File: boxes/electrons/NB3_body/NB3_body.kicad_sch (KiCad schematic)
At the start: 21 parts, among them J1 Conn_01x02_Male, J2 Conn_01x02_Male, J3 Conn_01x02_Male, J4 Conn_01x02_Male, J5 Conn_01x04_Male, J6 Conn_01x02_Male

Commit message: Work on NB3_body PCB...
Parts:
- removed C3, C4, C5: 10uF, Capacitor_SMD:C_0805_2012Metric, symbol Device:C
- removed F3, F4, F6: 1.1h2.2t, Fuse:Fuse_0805_2012Metric, symbol Device:Polyfuse
- removed F5: 3h5t, Fuse:Fuse_2920_7451Metric, symbol Device:Polyfuse
- removed J1, J2, J3, J4, J6: Conn_01x02_Male, Connector_PinHeader_2.54mm:PinHeader_1x02_P2.54mm_Vertical_SMD_Pin1Right, symbol Connector:Conn_01x02_Male
- removed J5: Conn_01x04_Male, Connector_PinHeader_2.54mm:PinHeader_1x04_P2.54mm_Vertical_SMD_Pin1Right, symbol Connector:Conn_01x04_Male
- added J1, J10, J2, J9: Conn_01x03_Female, Connector_PinHeader_2.54mm:PinHeader_1x03_P2.54mm_Vertical_SMD_Pin1Right, symbol Connector:Conn_01x03_Female
- added J11: Conn_02x10_Odd_Even, Connector_PinHeader_2.54mm:PinHeader_2x10_P2.54mm_Vertical_SMD, symbol Connector_Generic:Conn_02x10_Odd_Even
- added J12: Conn_01x04_Male, Connector_PinHeader_2.54mm:PinHeader_1x04_P2.54mm_Vertical_SMD_Pin1Right, symbol Connector:Conn_01x04_Male
- added J3, J4, J5, J6: Conn_01x10_Male, Connector_PinHeader_2.54mm:PinHeader_1x10_P2.54mm_Vertical_SMD_Pin1Right, symbol Connector:Conn_01x10_Male
- added J7, J8: Socket_SM06B-SRSS-TB, NB3_body:Socket_SM06B-SRSS-TB, symbol NB3_body:Socket_SM06B-SRSS-TB
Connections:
- removed net +5V: C1.1, C2.1, F1.2, F2.2
- net GND: no longer names the net of C2.2
- net GND: no longer C1.2
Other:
- note added: "Forebrain"
- note added: "Hindbrain"
- note added: "Midbrain"
- note added: "Pan-Tilit Servos"
- note added: "Thalamus"
- note removed: "Fuse: MF-LSMF300X-2"
- note removed: "Logic"
- note removed: "RPi"
- note removed: "Sensors"
- moved on the sheet: C1, C2, F1, F2

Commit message: Work on NB£_body PCB layout
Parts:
- removed J1, J10, J2, J9: Conn_01x03_Female, Connector_PinHeader_2.54mm:PinHeader_1x03_P2.54mm_Vertical_SMD_Pin1Right, symbol Connector:Conn_01x03_Female
- removed J11: Conn_02x10_Odd_Even, Connector_PinHeader_2.54mm:PinHeader_2x10_P2.54mm_Vertical_SMD, symbol Connector_Generic:Conn_02x10_Odd_Even
- removed J12: Conn_01x04_Male, Connector_PinHeader_2.54mm:PinHeader_1x04_P2.54mm_Vertical_SMD_Pin1Right, symbol Connector:Conn_01x04_Male
- removed J3, J4, J5, J6: Conn_01x10_Male, Connector_PinHeader_2.54mm:PinHeader_1x10_P2.54mm_Vertical_SMD_Pin1Right, symbol Connector:Conn_01x10_Male
- removed J7, J8: Socket_SM06B-SRSS-TB, NB3_body:Socket_SM06B-SRSS-TB, symbol NB3_body:Socket_SM06B-SRSS-TB
- added J1, J2, J3, J4, J5, J6, J7, J8: Conn_02x05_Counter_Clockwise, Connector_PinSocket_2.54mm:PinSocket_2x05_P2.54mm_Vertical_SMD, symbol Connector_Generic:Conn_02x05_Counter_Clockwise
- added J10, J11, J12: Conn_02x03_Top_Bottom, Connector_PinHeader_2.54mm:PinHeader_2x03_P2.54mm_Vertical_SMD, symbol Connector_Generic:Conn_02x03_Top_Bottom
- added J13, J14: JST ZH 6-way Socket, NB3_body:Connector_B6B-ZR-SM4-GW-TF(LF)(SN), symbol NB3_body:Connector_B6B-ZR-SM4-GW-TF(LF)(SN)
- added J9: JST SH 4-way Socket, NB3_body:Connector_S4B-PH-SM4-TB(LF)(SN), symbol NB3_body:Connector_S4B-PH-SM4-TB(LF)(SN)
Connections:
- new net +5V: J1.1 (Pin_1), J10.1 (Pin_1), J10.4 (Pin_4), J2.1 (Pin_1), J3.1 (Pin_1), J4.1 (Pin_1), J5.1 (Pin_1), J6.1 (Pin_1), J7.1 (Pin_1), J7.2 (Pin_2), J9.1, J9.2
- new net GND: J1.10 (Pin_10), J10.2 (Pin_2), J10.5 (Pin_5), J2.10 (Pin_10), J3.10 (Pin_10), J4.10 (Pin_10), J5.10 (Pin_10), J6.10 (Pin_10), J7.10 (Pin_10), J7.9 (Pin_9), J9.3, J9.4
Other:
- moved on the sheet: C1, C2, F1, F2

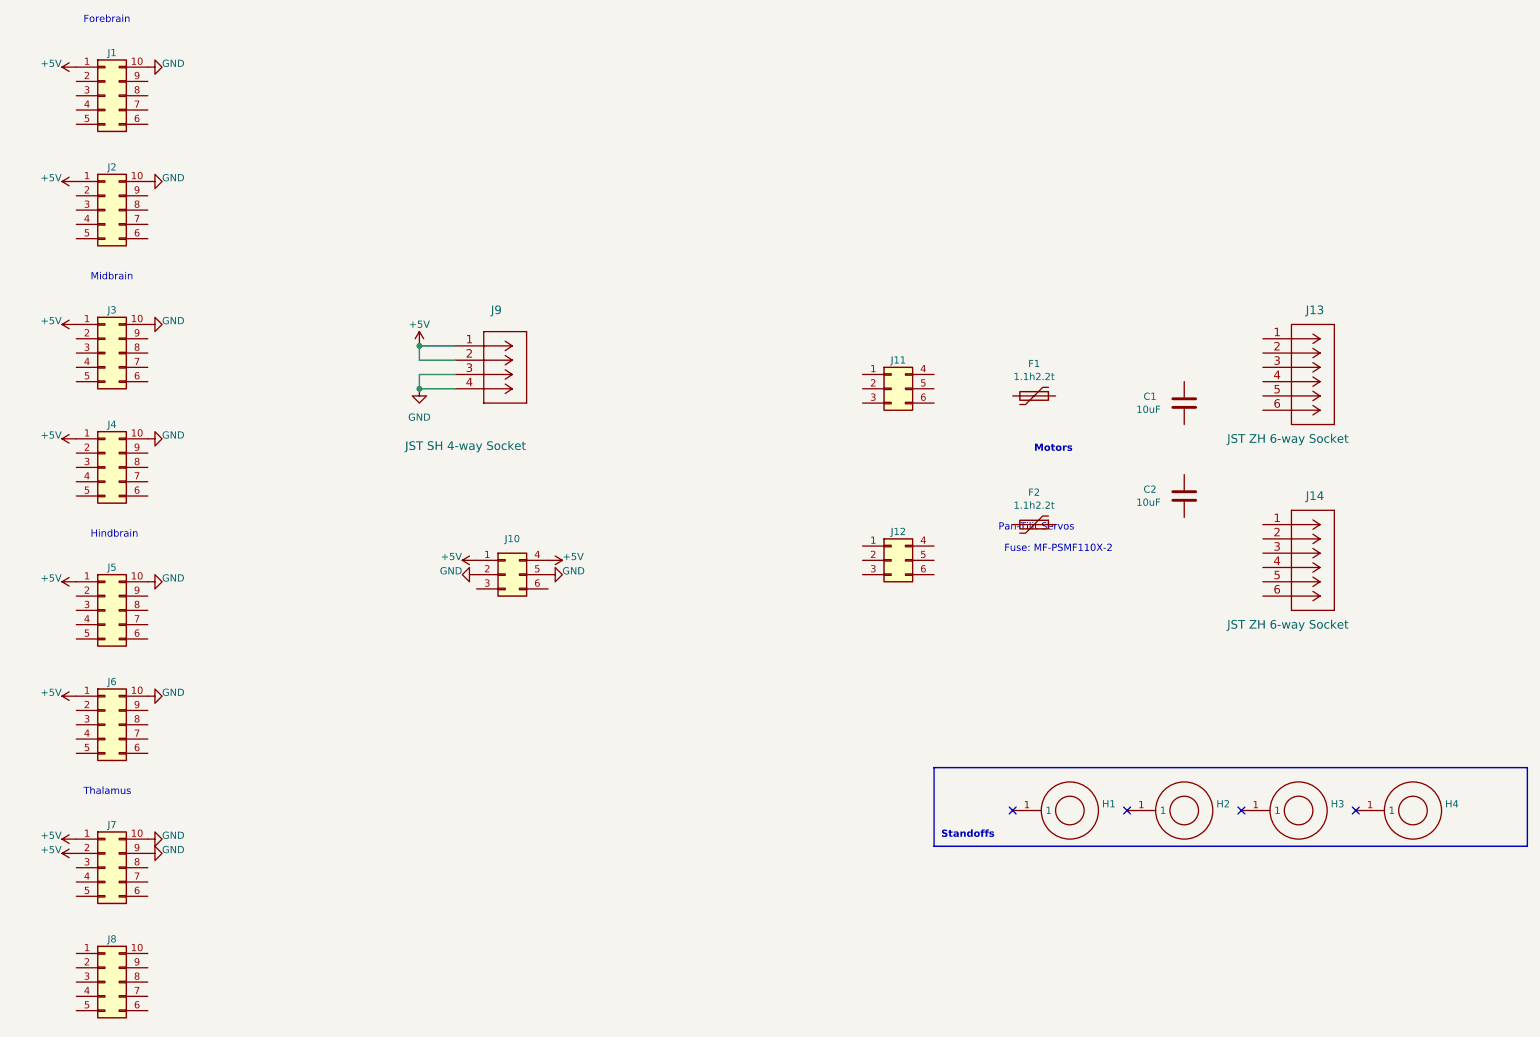
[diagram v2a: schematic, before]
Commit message: Work on NB3_body routing
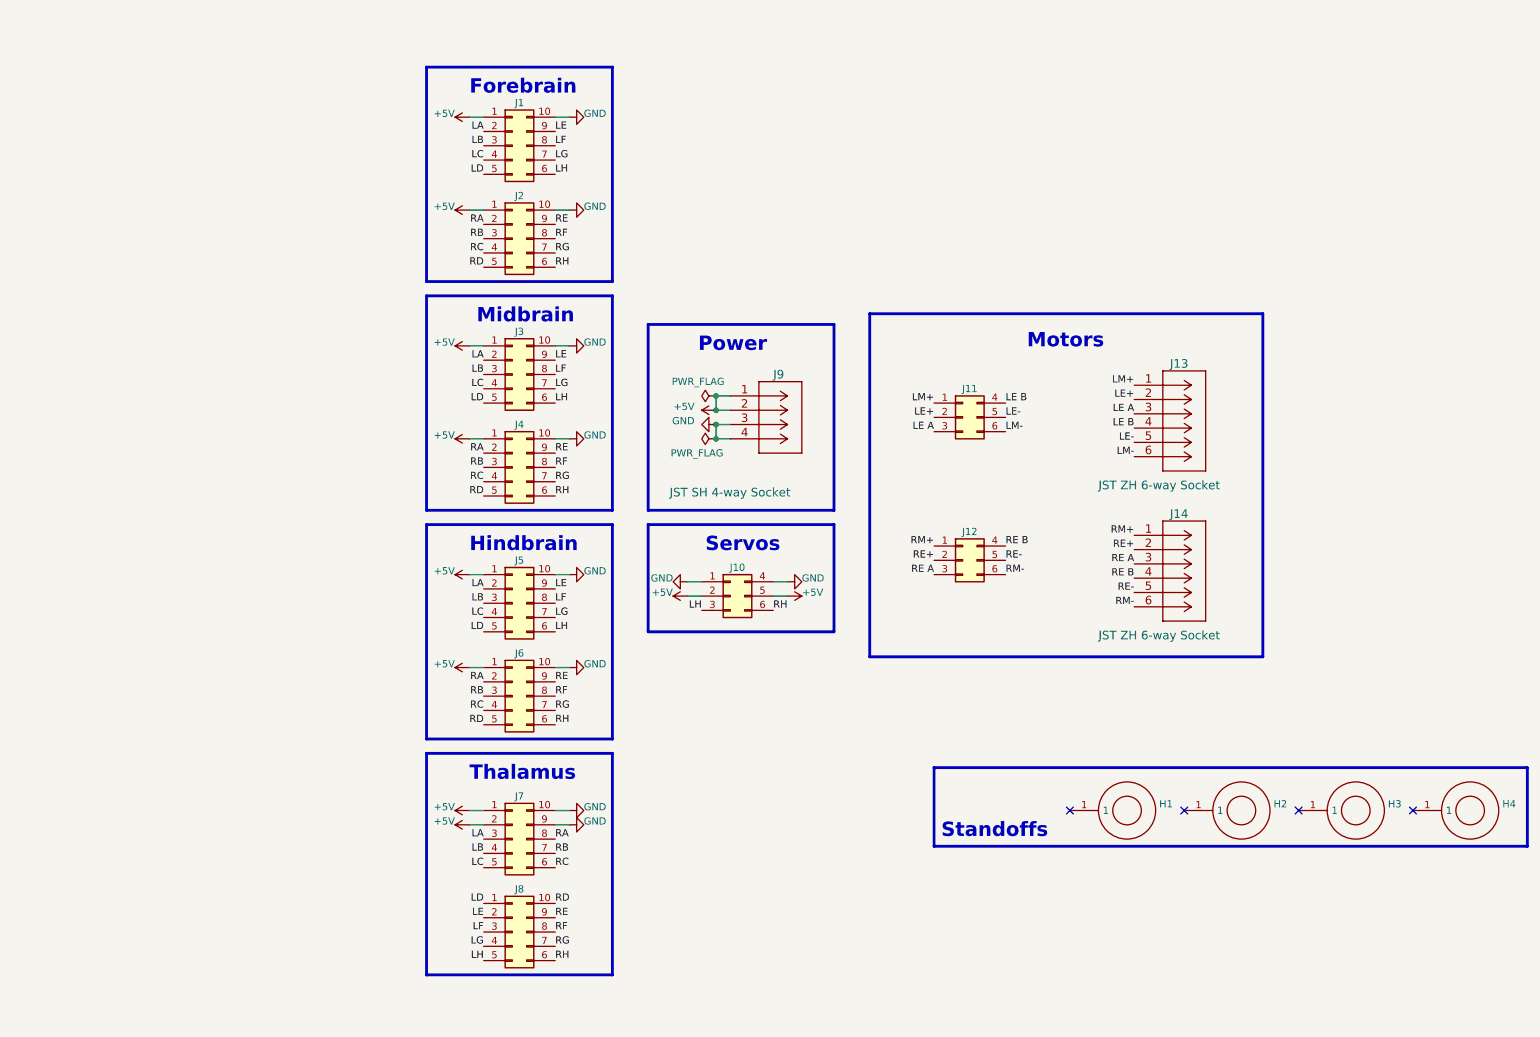
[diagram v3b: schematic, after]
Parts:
- removed C1, C2: 10uF, Capacitor_SMD:C_0805_2012Metric, symbol Device:C
- removed F1, F2: 1.1h2.2t, Fuse:Fuse_0805_2012Metric, symbol Device:Polyfuse
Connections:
- net +5V: now also J10.2 (Pin_2), J10.5 (Pin_5); no longer J10.1 (Pin_1), J10.4 (Pin_4)
- net GND: now also J10.1 (Pin_1), J10.4 (Pin_4); no longer J10.2 (Pin_2), J10.5 (Pin_5)
- net RM+: now reaches J14.1
- net RM+: now also J12.1 (Pin_1)
- net RE+: now reaches J14.2
- net RE+: now also J12.2 (Pin_2)
- net RE A: now reaches J14.3
- net RE A: now also J12.3 (Pin_3)
- net RE B: now reaches J14.4
- net RE B: now also J12.4 (Pin_4)
- net RE-: now reaches J14.5
- net RE-: now also J12.5 (Pin_5)
- net RM-: now reaches J14.6
- net RM-: now also J12.6 (Pin_6)
- net LM+: now reaches J11.1 (Pin_1)
- net LM+: now also J13.1
- net LE+: now reaches J11.2 (Pin_2)
- net LE+: now also J13.2
- net LE A: now reaches J11.3 (Pin_3)
- net LE A: now also J13.3
- net LE B: now reaches J11.4 (Pin_4)
- net LE B: now also J13.4
- net LE-: now reaches J11.5 (Pin_5)
- net LE-: now also J13.5
- net LM-: now reaches J11.6 (Pin_6)
- net LM-: now also J13.6
- net LA: now reaches J5.2 (Pin_2)
- net LA: now also J1.2 (Pin_2), J3.2 (Pin_2), J7.3 (Pin_3)
- net LB: now reaches J5.3 (Pin_3)
- net LB: now also J1.3 (Pin_3), J3.3 (Pin_3), J7.4 (Pin_4)
- net LC: now reaches J5.4 (Pin_4)
- net LC: now also J1.4 (Pin_4), J3.4 (Pin_4), J7.5 (Pin_5)
- net LD: now reaches J5.5 (Pin_5)
- net LD: now also J1.5 (Pin_5), J3.5 (Pin_5), J8.1 (Pin_1)
- net LH: now reaches J5.6 (Pin_6)
- net LH: now also J1.6 (Pin_6), J10.3 (Pin_3), J3.6 (Pin_6), J8.5 (Pin_5)
- net LG: now reaches J5.7 (Pin_7)
- net LG: now also J1.7 (Pin_7), J3.7 (Pin_7), J8.4 (Pin_4)
- net LF: now reaches J5.8 (Pin_8)
- net LF: now also J1.8 (Pin_8), J3.8 (Pin_8), J8.3 (Pin_3)
- net LE: now reaches J5.9 (Pin_9)
- net LE: now also J1.9 (Pin_9), J3.9 (Pin_9), J8.2 (Pin_2)
- net RA: now reaches J2.2 (Pin_2)
- net RA: now also J4.2 (Pin_2), J6.2 (Pin_2), J7.8 (Pin_8)
- net RB: now reaches J2.3 (Pin_3)
- net RB: now also J4.3 (Pin_3), J6.3 (Pin_3), J7.7 (Pin_7)
- net RC: now reaches J2.4 (Pin_4)
- net RC: now also J4.4 (Pin_4), J6.4 (Pin_4), J7.6 (Pin_6)
- net RD: now reaches J2.5 (Pin_5)
- net RD: now also J4.5 (Pin_5), J6.5 (Pin_5), J8.10 (Pin_10)
- net RH: now reaches J2.6 (Pin_6)
- net RH: now also J10.6 (Pin_6), J4.6 (Pin_6), J6.6 (Pin_6), J8.6 (Pin_6)
- net RG: now reaches J2.7 (Pin_7)
- net RG: now also J4.7 (Pin_7), J6.7 (Pin_7), J8.7 (Pin_7)
- net RF: now reaches J2.8 (Pin_8)
- net RF: now also J4.8 (Pin_8), J6.8 (Pin_8), J8.8 (Pin_8)
- net RE: now reaches J2.9 (Pin_9)
- net RE: now also J4.9 (Pin_9), J6.9 (Pin_9), J8.9 (Pin_9)
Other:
- note added: "Power"
- note added: "Servos"
- note removed: "Fuse: MF-PSMF110X-2"
- note removed: "Pan-Tilit Servos"
- moved on the sheet: H1, H2, H3, H4, J1, J10, J11, J12, J13, J14, J2, J3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

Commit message: NB3 pcb design tweaks
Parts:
- removed H1, H2, H3, H4: Standoff_SMT_5H_M2.5_9774050151R, NB3_body:Standoff_SMT_5H_M2.5_9774050151R, symbol NB3_body:Standoff_SMT_5H_M2.5_9774050151R
- added H1, H13, H14, H15, H16, H2, H3, H4, H5, H6, H7, H8: MountingHole, MountingHole:MountingHole_2.7mm_M2.5_ISO7380_Pad, symbol Mechanical:MountingHole
- added H10, H11, H12, H9: MountingHole, MountingHole:MountingHole_2.5mm_Pad, symbol Mechanical:MountingHole
- added H17, H18: MountingHole, MountingHole:MountingHole_2.2mm_M2_ISO7380_Pad, symbol Mechanical:MountingHole
- J1, J2, J3, J4, J5, J6, J7, J8: symbol Connector_Generic:Conn_02x05_Counter_Clockwise -> Connector_Generic:Conn_02x05_Odd_Even
- J10, J11, J12: symbol Connector_Generic:Conn_02x03_Top_Bottom -> Connector_Generic:Conn_02x03_Odd_Even
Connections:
- net +5V: now also J10.3 (Pin_3), J10.4 (Pin_4), J7.4 (Pin_4); no longer J10.2 (Pin_2), J10.5 (Pin_5), J7.1 (Pin_1)
- net GND: now also J1.2 (Pin_2), J10.2 (Pin_2), J2.2 (Pin_2), J3.2 (Pin_2), J4.2 (Pin_2), J5.2 (Pin_2), J6.2 (Pin_2), J7.1 (Pin_1), J7.3 (Pin_3); no longer J1.10 (Pin_10), J10.4 (Pin_4), J2.10 (Pin_10), J3.10 (Pin_10), J4.10 (Pin_10), J5.10 (Pin_10), J6.10 (Pin_10), J7.10 (Pin_10), J7.9 (Pin_9)
- net LA: now also J1.3 (Pin_3), J3.3 (Pin_3), J5.3 (Pin_3), J7.6 (Pin_6); no longer J1.2 (Pin_2), J3.2 (Pin_2), J5.2 (Pin_2), J7.3 (Pin_3)
- net LB: now also J1.5 (Pin_5), J3.5 (Pin_5), J5.5 (Pin_5), J7.8 (Pin_8); no longer J1.3 (Pin_3), J3.3 (Pin_3), J5.3 (Pin_3), J7.4 (Pin_4)
- net LC: now also J1.7 (Pin_7), J3.7 (Pin_7), J5.7 (Pin_7), J7.10 (Pin_10); no longer J1.4 (Pin_4), J3.4 (Pin_4), J5.4 (Pin_4), J7.5 (Pin_5)
- net LD: now also J1.9 (Pin_9), J3.9 (Pin_9), J5.9 (Pin_9), J8.2 (Pin_2); no longer J1.5 (Pin_5), J3.5 (Pin_5), J5.5 (Pin_5), J8.1 (Pin_1)
- net LE: now also J1.4 (Pin_4), J3.4 (Pin_4), J5.4 (Pin_4), J8.4 (Pin_4); no longer J1.9 (Pin_9), J3.9 (Pin_9), J5.9 (Pin_9), J8.2 (Pin_2)
- net LE A: now also J11.5 (Pin_5); no longer J11.3 (Pin_3)
- net LE B: now also J11.2 (Pin_2); no longer J11.4 (Pin_4)
- net LE+: now also J11.3 (Pin_3); no longer J11.2 (Pin_2)
- net LE-: now also J11.4 (Pin_4); no longer J11.5 (Pin_5)
- net LF: now also J1.6 (Pin_6), J3.6 (Pin_6), J5.6 (Pin_6), J8.6 (Pin_6); no longer J1.8 (Pin_8), J3.8 (Pin_8), J5.8 (Pin_8), J8.3 (Pin_3)
- net LG: now also J1.8 (Pin_8), J3.8 (Pin_8), J5.8 (Pin_8), J8.8 (Pin_8); no longer J1.7 (Pin_7), J3.7 (Pin_7), J5.7 (Pin_7), J8.4 (Pin_4)
- net LH: now also J1.10 (Pin_10), J10.5 (Pin_5), J3.10 (Pin_10), J5.10 (Pin_10), J8.10 (Pin_10); no longer J1.6 (Pin_6), J10.3 (Pin_3), J3.6 (Pin_6), J5.6 (Pin_6), J8.5 (Pin_5)
- net RA: now also J2.3 (Pin_3), J4.3 (Pin_3), J6.3 (Pin_3), J7.5 (Pin_5); no longer J2.2 (Pin_2), J4.2 (Pin_2), J6.2 (Pin_2), J7.8 (Pin_8)
- net RB: now also J2.5 (Pin_5), J4.5 (Pin_5), J6.5 (Pin_5); no longer J2.3 (Pin_3), J4.3 (Pin_3), J6.3 (Pin_3)
- net RC: now also J2.7 (Pin_7), J4.7 (Pin_7), J6.7 (Pin_7), J7.9 (Pin_9); no longer J2.4 (Pin_4), J4.4 (Pin_4), J6.4 (Pin_4), J7.6 (Pin_6)
- net RD: now also J2.9 (Pin_9), J4.9 (Pin_9), J6.9 (Pin_9), J8.1 (Pin_1); no longer J2.5 (Pin_5), J4.5 (Pin_5), J6.5 (Pin_5), J8.10 (Pin_10)
- net RE: now also J2.4 (Pin_4), J4.4 (Pin_4), J6.4 (Pin_4), J8.3 (Pin_3); no longer J2.9 (Pin_9), J4.9 (Pin_9), J6.9 (Pin_9), J8.9 (Pin_9)
- net RE A: now also J12.5 (Pin_5); no longer J12.3 (Pin_3)
- net RE B: now also J12.2 (Pin_2); no longer J12.4 (Pin_4)
- net RE+: now also J12.3 (Pin_3); no longer J12.2 (Pin_2)
- net RE-: now also J12.4 (Pin_4); no longer J12.5 (Pin_5)
- net RF: now also J2.6 (Pin_6), J4.6 (Pin_6), J6.6 (Pin_6), J8.5 (Pin_5); no longer J2.8 (Pin_8), J4.8 (Pin_8), J6.8 (Pin_8), J8.8 (Pin_8)
- net RG: now also J2.8 (Pin_8), J4.8 (Pin_8), J6.8 (Pin_8); no longer J2.7 (Pin_7), J4.7 (Pin_7), J6.7 (Pin_7)
- net RH: now also J2.10 (Pin_10), J4.10 (Pin_10), J6.10 (Pin_10), J8.9 (Pin_9); no longer J2.6 (Pin_6), J4.6 (Pin_6), J6.6 (Pin_6), J8.6 (Pin_6)
- no-connect marks 4 -> 0
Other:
- note added: "Mounting Holes"
- note removed: "Standoffs"
- moved on the sheet: J1, J10, J11, J12, J13, J14, J2, J3, J4, J5, J6, J7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

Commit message: Work on NB£_body PCB
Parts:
- added H19, H20: MountingHole, MountingHole:MountingHole_2.7mm_M2.5_ISO7380_Pad, symbol Mechanical:MountingHole
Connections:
- net +5V: now also J1.9 (Pin_9), J3.9 (Pin_9), J5.9 (Pin_9); no longer J1.1 (Pin_1), J3.1 (Pin_1), J5.1 (Pin_1)
- net GND: now also J1.10 (Pin_10), J3.10 (Pin_10), J5.10 (Pin_10); no longer J1.2 (Pin_2), J3.2 (Pin_2), J5.2 (Pin_2)
- net LA: now also J1.1 (Pin_1), J3.1 (Pin_1), J5.1 (Pin_1); no longer J1.3 (Pin_3), J3.3 (Pin_3), J5.3 (Pin_3)
- net LB: now also J1.3 (Pin_3), J3.3 (Pin_3), J5.3 (Pin_3); no longer J1.5 (Pin_5), J3.5 (Pin_5), J5.5 (Pin_5)
- net LC: now also J1.5 (Pin_5), J3.5 (Pin_5), J5.5 (Pin_5); no longer J1.7 (Pin_7), J3.7 (Pin_7), J5.7 (Pin_7)
- net LD: now also J1.7 (Pin_7), J3.7 (Pin_7), J5.7 (Pin_7); no longer J1.9 (Pin_9), J3.9 (Pin_9), J5.9 (Pin_9)
- net LE: now also J1.2 (Pin_2), J3.2 (Pin_2), J5.2 (Pin_2); no longer J1.4 (Pin_4), J3.4 (Pin_4), J5.4 (Pin_4)
- net LE A: now also J13.4; no longer J13.3
- net LE B: now also J13.3; no longer J13.4
- net LE+: now also J13.5; no longer J13.2
- net LE-: now also J13.2; no longer J13.5
- net LF: now also J1.4 (Pin_4), J3.4 (Pin_4), J5.4 (Pin_4); no longer J1.6 (Pin_6), J3.6 (Pin_6), J5.6 (Pin_6)
- net LG: now also J1.6 (Pin_6), J3.6 (Pin_6), J5.6 (Pin_6); no longer J1.8 (Pin_8), J3.8 (Pin_8), J5.8 (Pin_8)
- net LH: now also J1.8 (Pin_8), J3.8 (Pin_8), J5.8 (Pin_8); no longer J1.10 (Pin_10), J3.10 (Pin_10), J5.10 (Pin_10)
- net LM+: now also J13.6; no longer J13.1
- net LM-: now also J13.1; no longer J13.6
- net RE A: now also J12.6 (Pin_6); no longer J12.5 (Pin_5)
- net RE B: now also J12.1 (Pin_1); no longer J12.2 (Pin_2)
- net RE+: now also J12.4 (Pin_4); no longer J12.3 (Pin_3)
- net RE-: now also J12.3 (Pin_3); no longer J12.4 (Pin_4)
- net RM+: now also J12.2 (Pin_2); no longer J12.1 (Pin_1)
- net RM-: now also J12.5 (Pin_5); no longer J12.6 (Pin_6)
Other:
- moved on the sheet: H1, H10, H11, H12, H13, H14, H15, H16, H17, H18, H2, H3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

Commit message: Finished NB3_body PCB (pre-Fab)
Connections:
- net LE A: now also J13.3; no longer J13.4
- net LE B: now also J13.4; no longer J13.3
- net LE+: now also J13.2; no longer J13.5
- net LE-: now also J13.5; no longer J13.2
- net LM+: now also J13.1; no longer J13.6
- net LM-: now also J13.6; no longer J13.1
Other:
- moved on the sheet: H1, H10, H11, H12, H13, H14, H15, H16, H17, H18, H19, H2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
